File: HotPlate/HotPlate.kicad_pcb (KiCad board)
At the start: 2 copper layers, 61 parts, among them J1 USB_C_Receptacle_USB2.0_14P, J2 Heater, Q1 STU417S, Q4 MS50N06, SW1 RESET, SW2 BOOT, SW3 BTN0, SW4 BTN1, SW5 BTN2, SW6 BTN3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

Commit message: Finish routing
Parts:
- removed SW1: RESET, Button_Switch_SMD:SW_Push_1P1T_NO_CK_KMR2
- added RESET: RESET, Button_Switch_SMD:SW_Push_1P1T_NO_CK_KMR2, F.Cu at (144.3, 110.0)
- moved D2 75.6 mm to (146.2, 81.0), turned to -90 degrees
- moved R22 68.6 mm to (147.9, 81.0), turned to -90 degrees
- moved D1 57.8 mm to (169.7, 106.6), turned to 90 degrees
- moved C19 55.3 mm to (145.5, 93.0), turned to -90 degrees
- moved R21 54.6 mm to (168.0, 106.6), turned to 90 degrees
- moved R9 52.9 mm to (142.8, 100.5), turned to -90 degrees
- moved F1 50.5 mm to (171.0, 91.3), turned to 90 degrees
- moved R7 48.5 mm to (145.3, 103.3), turned to 180 degrees
- moved R15 47.7 mm to (159.4, 86.6)
- moved R2 47.5 mm to (144.4, 100.5), turned to -90 degrees
- moved C1 46.5 mm to (149.5, 100.9), turned to 90 degrees
- moved R14 44.4 mm to (162.3, 85.8), turned to 90 degrees
- moved TH1 39.1 mm to (177.8, 98.6), turned to 90 degrees
- moved J2 36.3 mm to (176.7, 81.0)
- moved SW5 32.6 mm to (120.7, 107.3)
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- renumbered SW2 to BOOT
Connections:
- net USBD+ renamed Net-(U1-USB_DP)
- net USBD- renamed Net-(U1-USB_DM)
- R21 pad 1: /STATUS -> +3V3
- U1 pad 27: /BTN0 -> unconnected-(U1-GPIO16-Pad27)
- U1 pad 28: /BTN1 -> /HOT
- U1 pad 29: /BTN2 -> /BTN0
- U1 pad 32: /STATUS -> unconnected-(U1-GPIO21-Pad32)
- U1 pad 34: /HOT -> unconnected-(U1-GPIO22-Pad34)
- U1 pad 39: unconnected-(U1-GPIO27/ADC1-Pad39) -> /BTN2
- U1 pad 41: unconnected-(U1-GPIO29/ADC3-Pad41) -> /BTN1
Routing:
- net +3V3: track 4.22 -> 223.4 mm, vias 0 -> 9
- net /THERM: track 0.00 -> 81.9 mm, vias 0 -> 2
- net /BTN2: track 7.97 -> 49.7 mm, vias 0 -> 2
- net Net-(Q1-G): track 0.00 -> 33.8 mm, vias 0 -> 2
- net /SS: track 1.80 -> 35.5 mm, vias 0 -> 2
- net /BTN1: track 7.77 -> 34.2 mm, vias 0 -> 2
- net /RESET: track 6.15 -> 32.5 mm, vias 0 -> 2
- net /SDA: track 0.00 -> 26.0 mm, vias 0 -> 4
- net /BTN3: track 7.95 -> 32.1 mm
- net +1V1: track 0.00 -> 21.5 mm
- net /SCL: track 0.00 -> 21.3 mm
- net /VBUS: track 16.4 -> 36.6 mm, vias 0 -> 2
- net GND: track 0.14 -> 18.4 mm, vias 0 -> 3
- net /SD1: track 0.00 -> 15.2 mm, vias 0 -> 2
- net /SD2: track 0.00 -> 15.1 mm, vias 0 -> 2
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- added copper zone on B.Cu, net GND
- added copper zone on F.Cu, net GND
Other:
- board outline added: 64 x 39 mm
- board text added: "20V+"

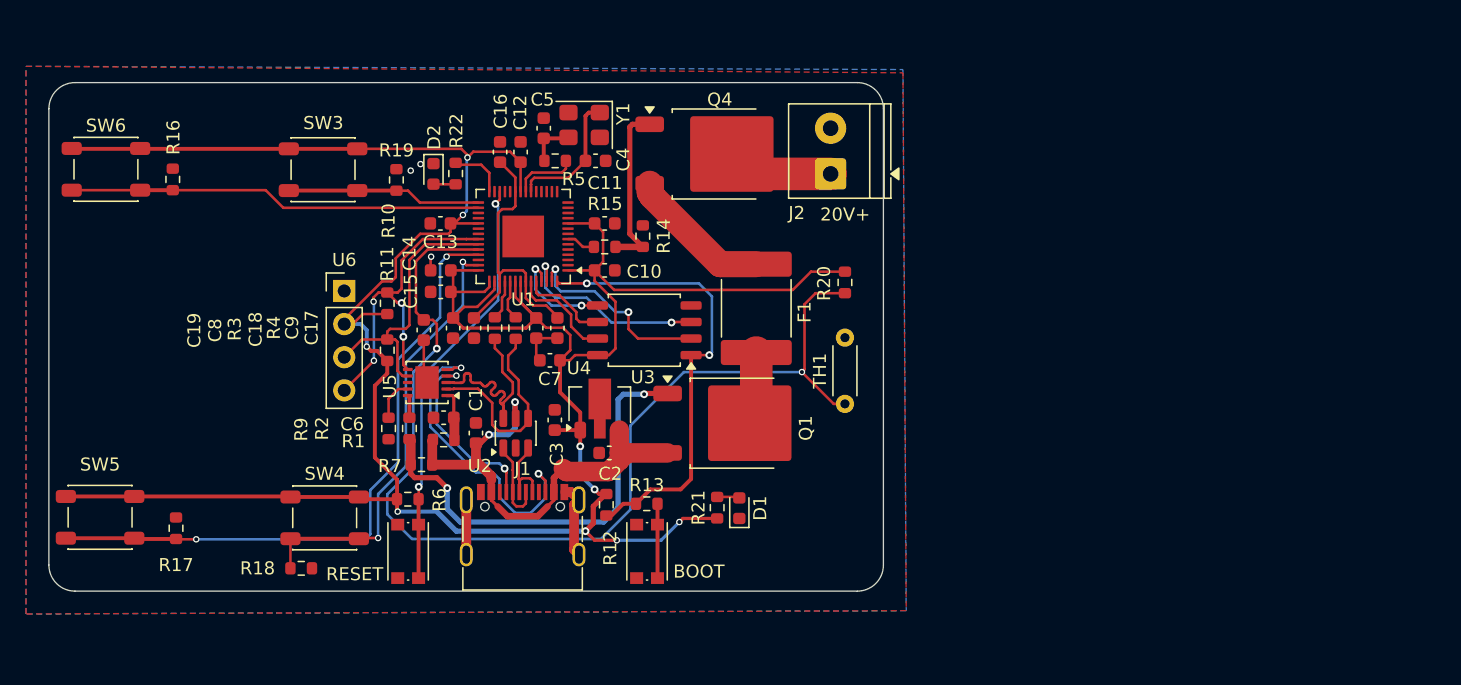
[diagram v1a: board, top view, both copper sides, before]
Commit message: Minor placement changes and ground vias
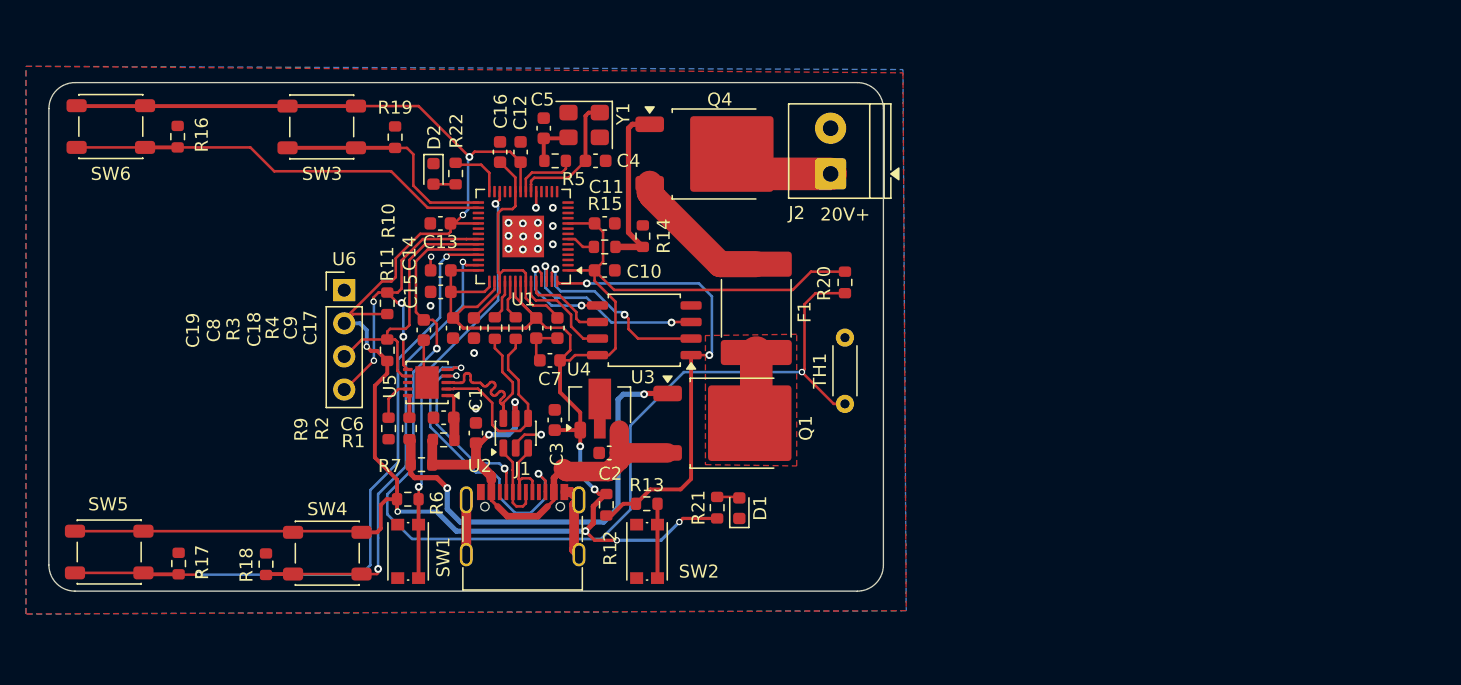
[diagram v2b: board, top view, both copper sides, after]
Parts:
- moved R16 3.30 mm to (126.6, 78.1)
- moved SW6 3.30 mm to (121.5, 77.4)
- moved R19 3.28 mm to (143.3, 78.2)
- moved SW3 3.28 mm to (137.7, 77.4)
- moved SW5 2.75 mm to (121.4, 110.0)
- moved R18 2.72 mm to (133.4, 110.9), turned to 90 degrees
- moved R17 2.72 mm to (126.7, 110.9)
- moved SW4 2.72 mm to (138.1, 110.1)
- moved U6 0.06 mm to (139.4, 89.9)
- renumbered RESET to SW1, BOOT to SW2
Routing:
- net GND: track 18.4 -> 22.2 mm, vias 3 -> 18
- net +3V3: track 223.4 -> 227.1 mm
- net /BTN0: track 14.9 -> 17.8 mm
- net /BTN1: track 34.2 -> 36.5 mm
- net /BTN2: track 49.7 -> 52.1 mm
- net /BTN3: track 32.1 -> 33.1 mm
- added copper zone on F.Cu, net +15V

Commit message: Started Code and Added Name to PCB
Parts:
- U6: moved to B.Cu
- turned U6 to 180 degrees
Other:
- board text added: "Dynix"

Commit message: Minor code changes
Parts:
- renumbered SW2 to BOOT, SW3 to BTN0, SW4 to BTN1, SW5 to BTN2, SW6 to BTN3, SW1 to RESET
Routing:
- net GND: track 22.2 -> 23.6 mm

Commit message: code for screen
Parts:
- renumbered D2 to HOT, D1 to STATUS
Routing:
- net /VBUS: track 36.6 -> 38.7 mm
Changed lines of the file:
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@@
 		(descr "Diode SMD 0603 (1608 Metric), square (rectangular) end terminal, IPC-7351 nominal, (Body size source: http://www.tortai-tech.com/upload/download/2011102023233369053.pdf), generated with kicad-footprint-generator")
 		(tags "diode")
-		(property "Reference" "D1"
+		(property "Reference" "STATUS"
 			(at 0 1.6 90)
 			(layer "F.SilkS")
@@
 		(descr "Diode SMD 0603 (1608 Metric), square (rectangular) end terminal, IPC-7351 nominal, (Body size source: http://www.tortai-tech.com/upload/download/2011102023233369053.pdf), generated with kicad-footprint-generator")
 		(tags "diode")
-		(property "Reference" "D2"
-			(at -2.8 -0.05625 90)
+		(property "Reference" "HOT"
+			(at -3.25 -0.05625 90)
 			(layer "F.SilkS")
 			(effects
@@
 		(embedded_fonts no)
 		(model "${KICAD9_3DMODEL_DIR}/Connector_PinHeader_2.54mm.3dshapes/PinHeader_1x04_P2.54mm_Vertical.step"
+			(hide yes)
 			(offset
 				(xyz 0 0 0)
@@
 		)
 	)
-	(gr_line
+	(gr_arc
 		(start 116.75 76)
-		(end 116.75 111)
+		(mid 117.335786 74.585786)
+		(end 118.75 74)
 		(stroke
 			(width 0.05)
@@
 		(layer "Edge.Cuts")
 	)
-	(gr_arc
-		(start 116.75 76)
-		(mid 117.335786 74.585786)
-		(end 118.75 74)
+	(gr_line
+		(start 116.75 111)
+		(end 116.75 76)
 		(stroke
 			(width 0.05)
@@
 	)
 	(segment
+		(start 155.48 105.4)
+		(end 155.48 104.7)
+		(width 0.5)
+		(layer "F.Cu")
+		(net "/VBUS")
+	)
+	(segment
 		(start 160.5 102.4)
 		(end 160.5 100.65)
@@
 	)
 	(segment
+		(start 155.48 104.55)
+		(end 155.48 104.38)
+		(width 0.5)
+		(layer "F.Cu")
+		(net "/VBUS")
+	)
+	(segment
 		(start 152.5 99.7)
 		(end 152.55 99.75)
@@
 	)
 	(segment
+		(start 155.48 104.7)
+		(end 155.48 104.55)
+		(width 0.5)
+		(layer "F.Cu")
+		(net "/VBUS")
+	)
+	(segment
 		(start 149.2 103.3)
 		(end 149.5 103)
@@
 	)
 	(segment
+		(start 155.48 104.32)
+		(end 155.48 103.82)
+		(width 0.5)
+		(layer "F.Cu")
+		(net "/VBUS")
+	)
+	(segment
 		(start 152.5 98.5)
 		(end 152.5 99.7)
@@
 	)
 	(segment
+		(start 156.204 103.826)
+		(end 156.426 103.826)
+		(width 0.5)
+		(layer "F.Cu")
+		(net "/VBUS")
+	)
+	(segment
 		(start 146.15 103.3)
 		(end 146.15 101.45)
@@
 	)
 	(segment
-		(start 155.48 105.4)
+		(start 155.48 104.7)
 		(end 155.48 104.32)
 		(width 0.5)
@@
 	)
 	(segment
+		(start 155.48 103.82)
+		(end 155.55 103.75)
+		(width 0.5)
+		(layer "F.Cu")
+		(net "/VBUS")
+	)
+	(segment
 		(start 161.09435 102.4)
 		(end 164.2 102.4)
@@
 		(layer "F.Cu")
 		(net "/VBUS")
+	)
+	(segment
+		(start 155.48 104.55)
+		(end 156.204 103.826)
+		(width 0.5)
+		(layer "F.Cu")
+		(net "/VBUS")

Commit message: add ibom
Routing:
- net /VBUS: track 38.7 -> 23.4 mm
- net +15V: track 5.63 -> 0.71 mm
- net GND: vias 18 -> 60
- added copper zone on F.Cu, net /VBUS

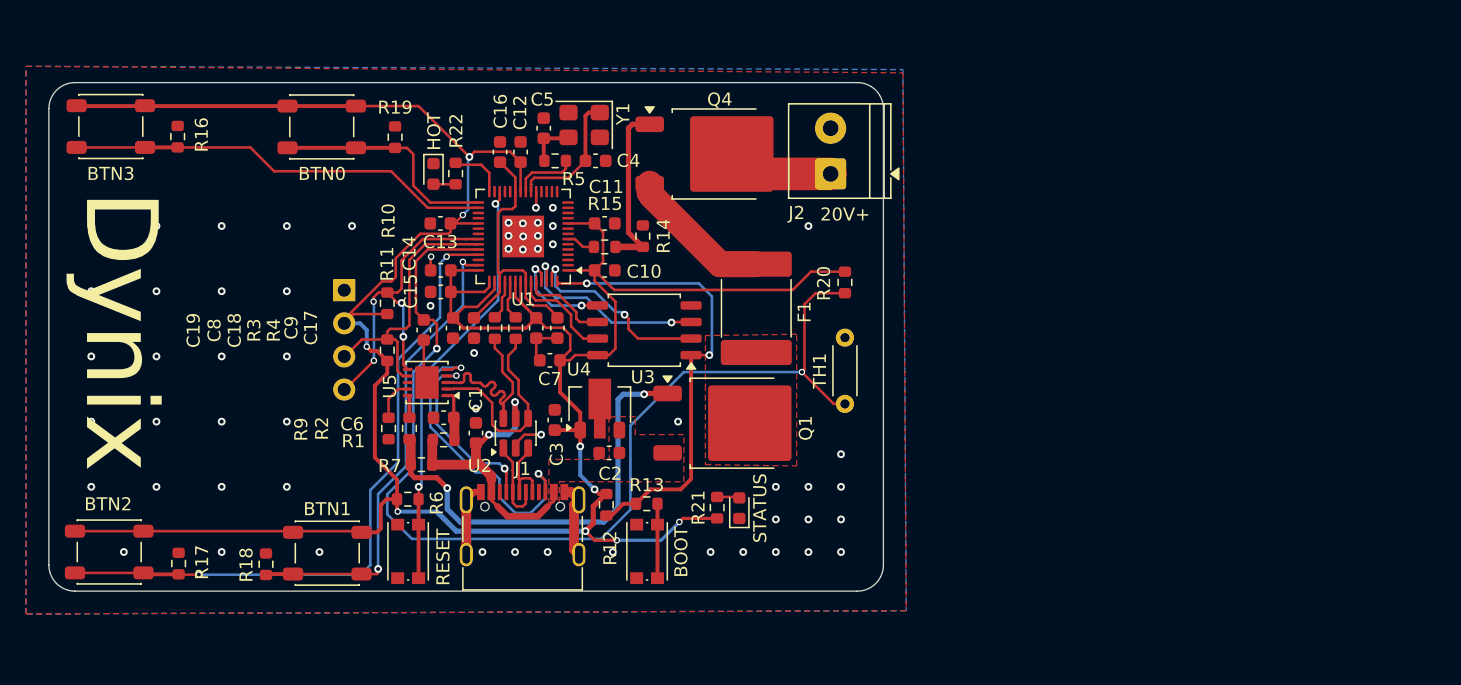
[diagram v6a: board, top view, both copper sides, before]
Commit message: Change LED size
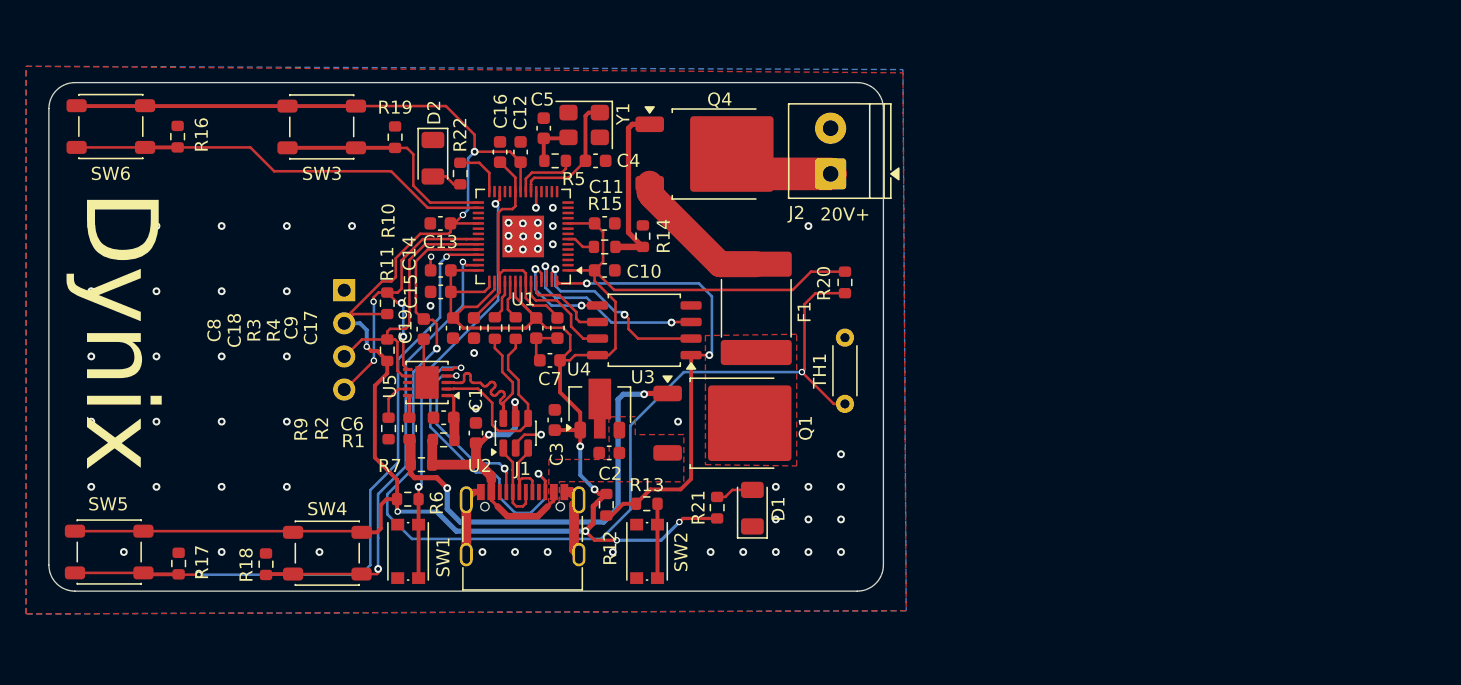
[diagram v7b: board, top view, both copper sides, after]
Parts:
- D1: renamed from STATUS; footprint Diode_SMD:D_0603_1608Metric -> Diode_SMD:D_1206_3216Metric
- D2: renamed from HOT; footprint Diode_SMD:D_0603_1608Metric -> Diode_SMD:D_1206_3216Metric
- moved D2 1.20 mm to (146.2, 79.8)
- moved D1 1.00 mm to (170.7, 106.6)
- moved R22 0.36 mm to (148.3, 81.0)
- moved C19 0.07 mm to (145.5, 92.9)
- renumbered RESET to SW1, BOOT to SW2, BTN0 to SW3, BTN1 to SW4, BTN2 to SW5, BTN3 to SW6
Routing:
- net Net-(D1-A): track 1.73 -> 2.92 mm
- net +3V3: track 227.1 -> 228.1 mm
- net Net-(D2-A): track 1.69 -> 2.35 mm

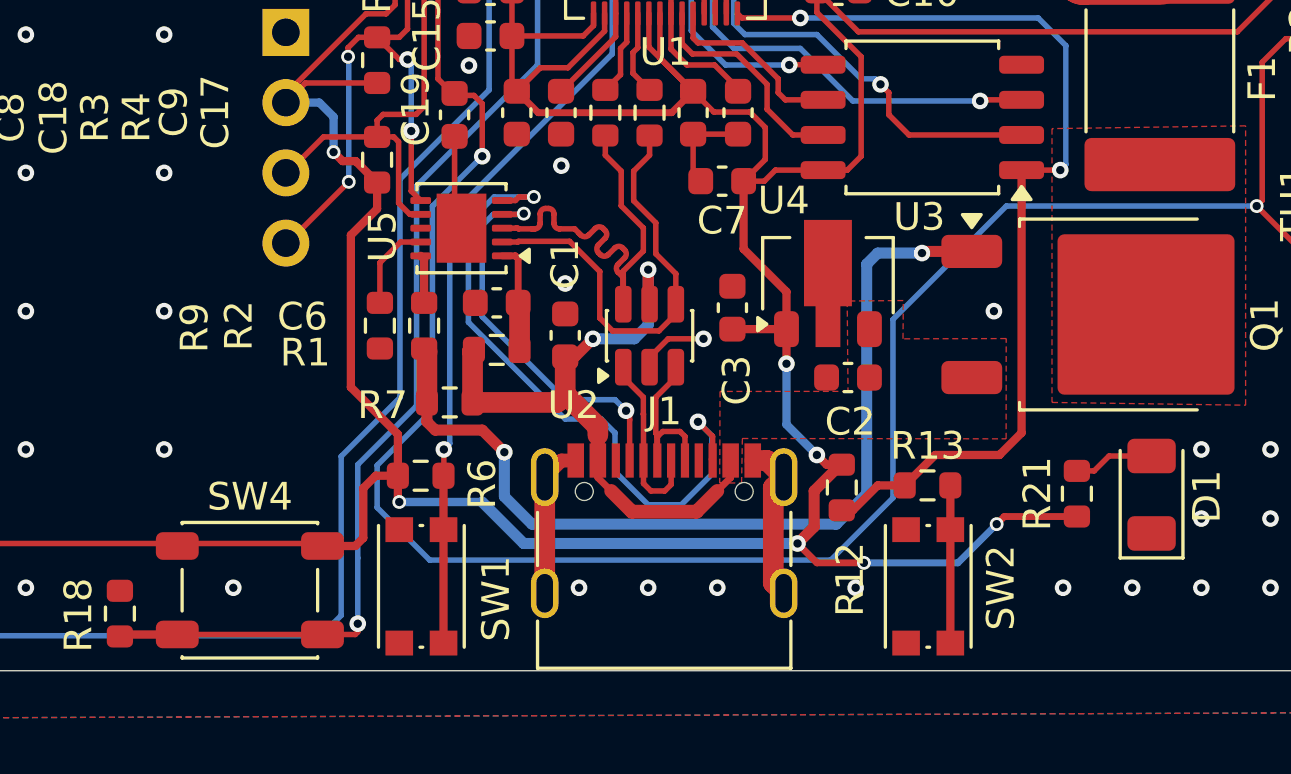
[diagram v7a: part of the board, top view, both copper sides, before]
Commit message: Change button footprint
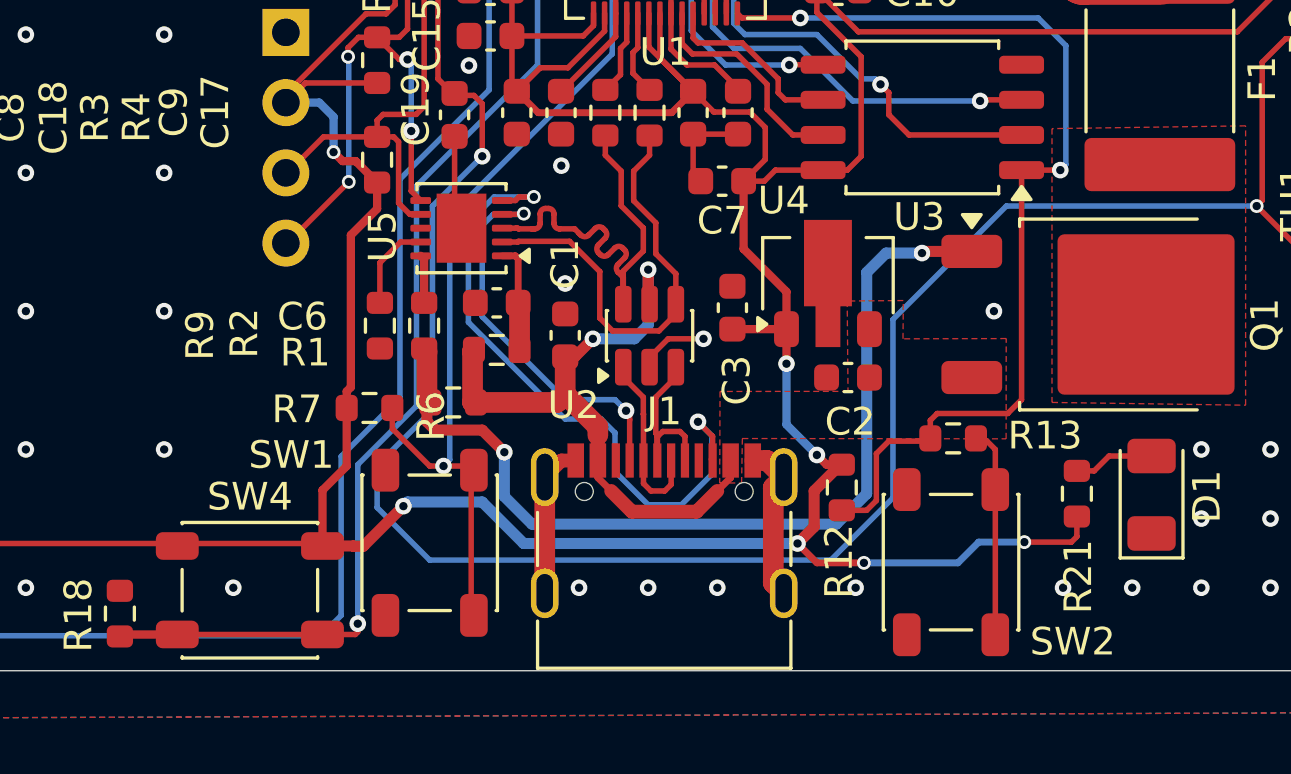
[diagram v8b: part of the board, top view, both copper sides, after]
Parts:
- SW1, SW2: footprint Button_Switch_SMD:SW_Push_1P1T_NO_CK_KMR2 -> Button_Switch_SMD:SW_SPST_PTS647_Sx38
- moved R6 3.07 mm to (142.4, 103.5)
- moved R13 1.94 mm to (163.5, 104.6)
- moved SW1 1.60 mm to (144.6, 108.4)
- moved SW2 1.20 mm to (163.4, 109.1)
- moved R7 0.12 mm to (145.4, 103.3)
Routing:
- net /RESET: track 32.5 -> 35.4 mm
- net Net-(R13-Pad2): track 5.95 -> 7.67 mm
- net /SS: track 35.5 -> 36.2 mm
